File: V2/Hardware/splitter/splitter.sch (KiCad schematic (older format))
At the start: 17 parts, among them J0 Rpi_40Pin_F, J1 Control_seg:1, J2 Control_seg:2, J3 Control_seg:3, J4 Molex_PSU_F, J5 Siren, J6 USB_A_F, K0 RELRAS0515, Q1 BD139-16

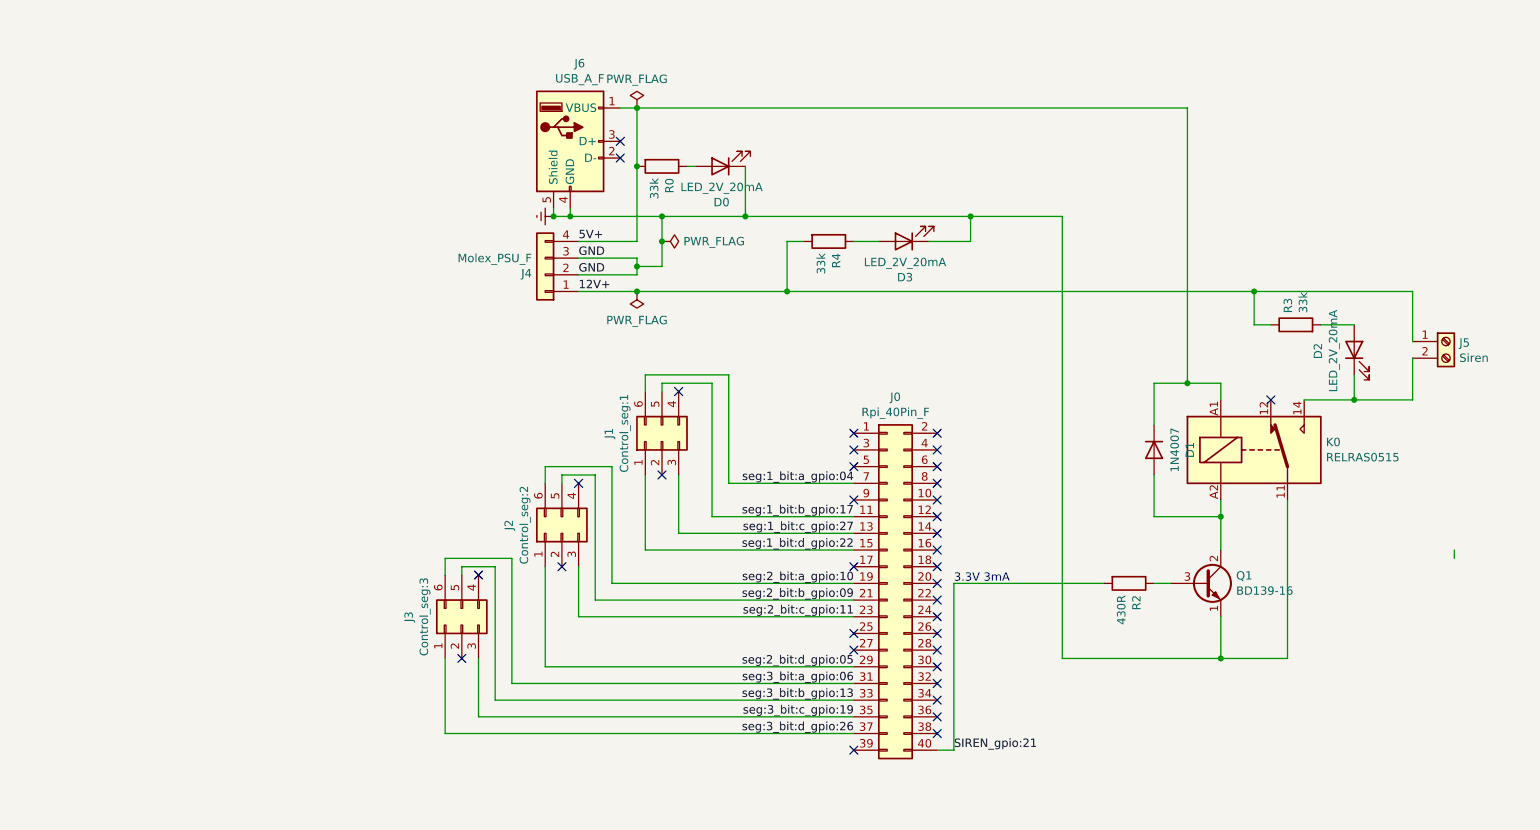
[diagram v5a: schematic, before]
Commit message: Add bypass caps and filtering
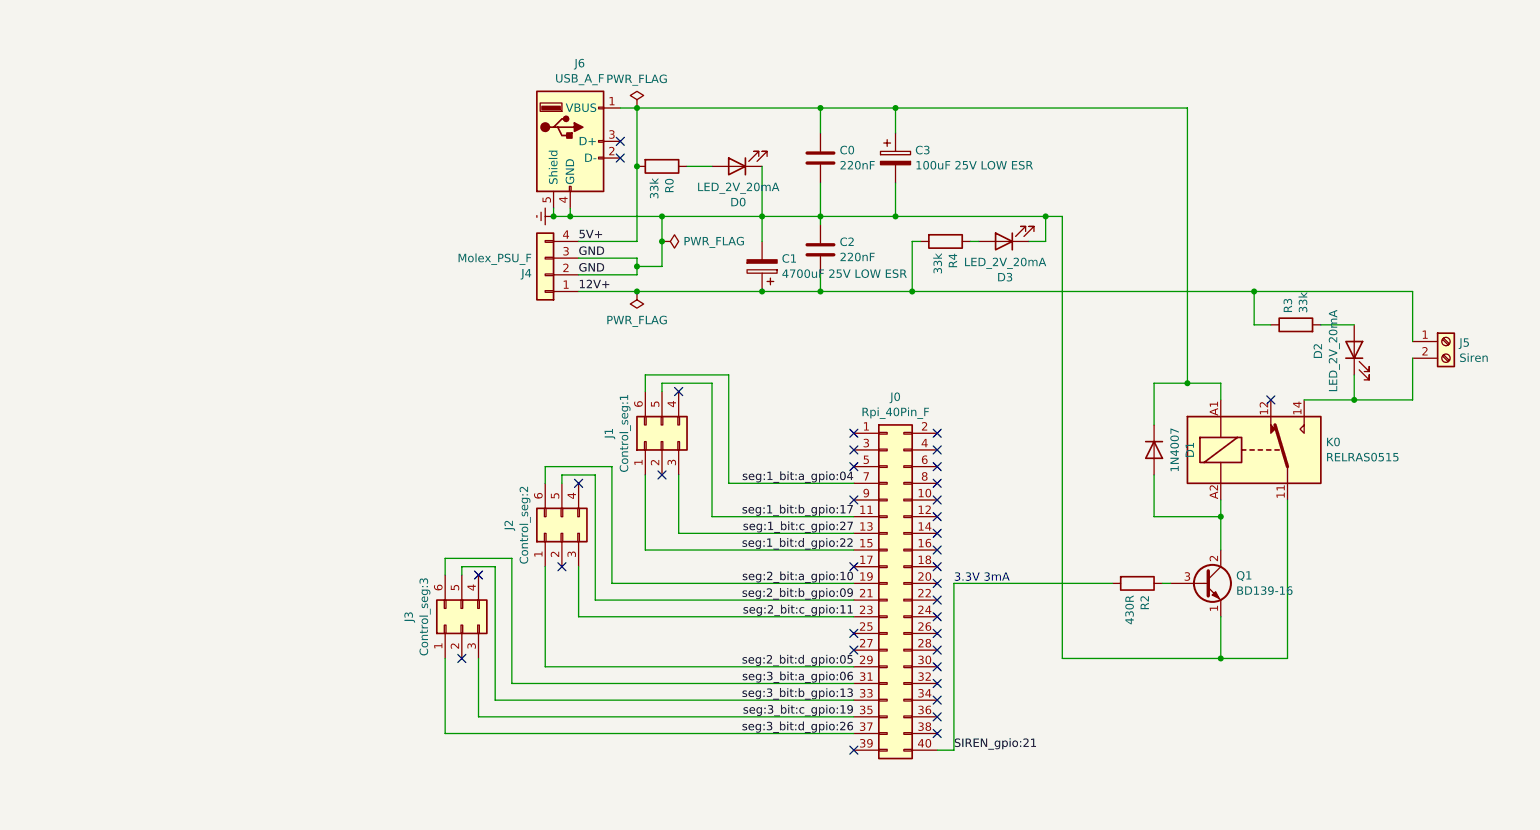
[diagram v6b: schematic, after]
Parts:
- added C0, C2: 220nF, Capacitor_THT:C_Disc_D4.3mm_W1.9mm_P5.00mm, symbol Device:C
- added C1: 4700uF 25V LOW ESR, Capacitor_THT:CP_Radial_D18.0mm_P7.50mm, symbol Device:CP
- added C3: 100uF 25V LOW ESR, Capacitor_THT:CP_Radial_D10.0mm_P5.00mm, symbol Device:CP
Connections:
- net 12V+: now also C1.1, C2.2
- net 5V+: now also C0.1, C3.1
- net Earth: now also C0.2, C1.2, C2.1, C3.2
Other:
- moved on the sheet: D0, D3, R2, R4
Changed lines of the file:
@@
 L Device:LED D0
 U 1 1 5EC196E4
-P 4800 2100
-F 0 "D0" H 4793 2316 50  0000 C CNN
-F 1 "LED_2V_20mA" H 4793 2225 50  0000 C CNN
-F 2 "LED_THT:LED_D5.0mm" H 4800 2100 50  0001 C CNN
-F 3 "~" H 4800 2100 50  0001 C CNN
-	1    4800 2100
+P 4900 2100
+F 0 "D0" H 4893 2316 50  0000 C CNN
+F 1 "LED_2V_20mA" H 4893 2225 50  0000 C CNN
+F 2 "LED_THT:LED_D5.0mm" H 4900 2100 50  0001 C CNN
+F 3 "~" H 4900 2100 50  0001 C CNN
+	1    4900 2100
 	-1   0    0    1
 $EndComp
@@
 	4450 2550 4450 2400
 Wire Wire Line
-	4450 2400 4950 2400
+	4450 2400 5050 2400
 Connection ~ 4450 2400
 Connection ~ 4300 2100
@@
 	4300 2100 4300 1750
 Wire Wire Line
-	4600 2100 4650 2100
-Wire Wire Line
-	4950 2100 4950 2400
-Connection ~ 4950 2400
+	4600 2100 4750 2100
+Wire Wire Line
+	5050 2100 5050 2400
+Connection ~ 5050 2400
 $Comp
 L power:PWR_FLAG #FLG0103
@@
 L Device:R R2
 U 1 1 5ED47928
-P 7250 4600
-F 0 "R2" H 7320 4646 50  0000 L CNN
-F 1 "430R" H 7320 4555 50  0000 L CNN
-F 2 "Resistor_THT:R_Axial_DIN0207_L6.3mm_D2.5mm_P10.16mm_Horizontal" V 7180 4600 50  0001 C CNN
-F 3 "~" H 7250 4600 50  0001 C CNN
-	1    7250 4600
+P 7300 4600
+F 0 "R2" H 7370 4646 50  0000 L CNN
+F 1 "430R" H 7370 4555 50  0000 L CNN
+F 2 "Resistor_THT:R_Axial_DIN0207_L6.3mm_D2.5mm_P10.16mm_Horizontal" V 7230 4600 50  0001 C CNN
+F 3 "~" H 7300 4600 50  0001 C CNN
+	1    7300 4600
 	0    1    1    0
 $EndComp
@@
 $EndComp
 Wire Wire Line
-	7400 4600 7500 4600
-Wire Wire Line
-	4300 2850 5200 2850
-Wire Wire Line
-	6850 2400 6850 5050
+	7450 4600 7500 4600
+Wire Wire Line
+	4300 2850 5050 2850
 Wire Wire Line
 	6850 5050 7800 5050
 Wire Wire Line
 	7800 5050 7800 4800
-Wire Wire Line
-	4950 2400 6300 2400
 Wire Wire Line
 	7800 4100 7800 4200
@@
 	0    -1   -1   0
 $EndComp
-Wire Wire Line
-	9200 4450 9200 4400
 NoConn ~ 6100 4200
 $Comp
@@
 L Device:R R4
 U 1 1 5FCA692B
-P 5450 2550
-F 0 "R4" H 5520 2596 50  0000 L CNN
-F 1 "33k" H 5520 2505 50  0000 L CNN
-F 2 "Resistor_THT:R_Axial_DIN0207_L6.3mm_D2.5mm_P10.16mm_Horizontal" V 5380 2550 50  0001 C CNN
-F 3 "~" H 5450 2550 50  0001 C CNN
-	1    5450 2550
+P 6150 2550
+F 0 "R4" H 6220 2596 50  0000 L CNN
+F 1 "33k" H 6220 2505 50  0000 L CNN
+F 2 "Resistor_THT:R_Axial_DIN0207_L6.3mm_D2.5mm_P10.16mm_Horizontal" V 6080 2550 50  0001 C CNN
+F 3 "~" H 6150 2550 50  0001 C CNN
+	1    6150 2550
 	0    1    1    0
 $EndComp
@@
 L Device:LED D3
 U 1 1 5FCABBDF
-P 5900 2550
-F 0 "D3" H 5893 2766 50  0000 C CNN
-F 1 "LED_2V_20mA" H 5893 2675 50  0000 C CNN
-F 2 "LED_THT:LED_D5.0mm" H 5900 2550 50  0001 C CNN
-F 3 "~" H 5900 2550 50  0001 C CNN
-	1    5900 2550
+P 6500 2550
+F 0 "D3" H 6493 2766 50  0000 C CNN
+F 1 "LED_2V_20mA" H 6493 2675 50  0000 C CNN
+F 2 "LED_THT:LED_D5.0mm" H 6500 2550 50  0001 C CNN
+F 3 "~" H 6500 2550 50  0001 C CNN
+	1    6500 2550
 	-1   0    0    1
 $EndComp
 Wire Wire Line
-	5200 2850 5200 2550
-Wire Wire Line
-	5200 2550 5300 2550
-Connection ~ 5200 2850
-Wire Wire Line
-	5600 2550 5750 2550
-Wire Wire Line
-	6050 2550 6300 2550
-Wire Wire Line
-	6300 2550 6300 2400
-Connection ~ 6300 2400
-Wire Wire Line
-	6300 2400 6850 2400
+	5950 2850 5950 2550
+Wire Wire Line
+	5950 2550 6000 2550
+Connection ~ 5950 2850
+Wire Wire Line
+	6300 2550 6350 2550
+Wire Wire Line
+	6650 2550 6750 2550
+Wire Wire Line
+	6750 2550 6750 2400
+Connection ~ 6750 2400
+Wire Wire Line
+	6750 2400 6850 2400
 Wire Wire Line
 	4850 4000 5600 4000
@@
 NoConn ~ 3250 5050
 Wire Wire Line
-	6200 4600 7100 4600
+	6200 4600 7150 4600
 Wire Wire Line
 	7600 3400 7600 1750
 Wire Wire Line
-	4300 1750 7600 1750
+	4300 1750 5400 1750
 Connection ~ 7600 3400
 Wire Wire Line
@@
 Wire Wire Line
 	8950 2850 8950 3150
-Wire Wire Line
-	5200 2850 8000 2850
 Wire Wire Line
 	8300 3500 8600 3500
@@
 Text Notes 6200 4600 0    50   ~ 0
 3.3V 3mA
+$Comp
+L Device:CP C1
+U 1 1 5FDD03EF
+P 5050 2700
+F 0 "C1" H 4932 2654 50  0000 R CNN
+F 1 "4700uF 25V LOW ESR" H 4932 2745 50  0000 R CNN
+F 2 "Capacitor_THT:CP_Radial_D18.0mm_P7.50mm" H 5088 2550 50  0001 C CNN
+F 3 "~" H 5050 2700 50  0001 C CNN
+	1    5050 2700
+	-1   0    0    1
+$EndComp
+Wire Wire Line
+	5050 2550 5050 2400
+Wire Wire Line
+	5050 2400 5400 2400
+Connection ~ 5050 2850
+Wire Wire Line
+	5050 2850 5400 2850
+$Comp
+L Device:C C2
+U 1 1 5FE2424F
+P 5400 2600
+F 0 "C2" H 5515 2646 50  0000 L CNN
+F 1 "220nF" H 5515 2555 50  0000 L CNN
+F 2 "Capacitor_THT:C_Disc_D4.3mm_W1.9mm_P5.00mm" H 5438 2450 50  0001 C CNN
+F 3 "~" H 5400 2600 50  0001 C CNN
+	1    5400 2600
+	1    0    0    -1
+$EndComp
+Wire Wire Line
+	5400 2450 5400 2400
+Connection ~ 5400 2400
+Wire Wire Line
+	5400 2400 5850 2400
+Wire Wire Line
+	5400 2750 5400 2850
+Connection ~ 5400 2850
+Wire Wire Line
+	5400 2850 5950 2850
+$Comp
+L Device:C C0
+U 1 1 5FE2BD03
+P 5400 2050
+F 0 "C0" H 5515 2096 50  0000 L CNN
+F 1 "220nF" H 5515 2005 50  0000 L CNN
+F 2 "Capacitor_THT:C_Disc_D4.3mm_W1.9mm_P5.00mm" H 5438 1900 50  0001 C CNN
+F 3 "~" H 5400 2050 50  0001 C CNN
+	1    5400 2050
+	1    0    0    -1
+$EndComp
+Connection ~ 5400 1750
+Wire Wire Line
+	5400 1750 5850 1750
+Wire Wire Line
+	5400 1750 5400 1900
+Wire Wire Line
+	5400 2200 5400 2400
+$Comp
+L Device:CP C3
+U 1 1 5FE36909
+P 5850 2050
+F 0 "C3" H 5968 2096 50  0000 L CNN
+F 1 "100uF 25V LOW ESR" H 5968 2005 50  0000 L CNN
+F 2 "Capacitor_THT:CP_Radial_D10.0mm_P5.00mm" H 5888 1900 50  0001 C CNN
+F 3 "~" H 5850 2050 50  0001 C CNN
+	1    5850 2050
+	1    0    0    -1
+$EndComp
+Wire Wire Line
+	5850 1900 5850 1750
+Connection ~ 5850 1750
+Wire Wire Line
+	5850 1750 7600 1750
+Wire Wire Line
+	5850 2200 5850 2400
+Connection ~ 5850 2400
+Wire Wire Line
+	5850 2400 6750 2400
+Wire Wire Line
+	5950 2850 8000 2850
+Wire Wire Line
+	6850 2400 6850 5050
 $EndSCHEMATC

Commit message: Update splitter
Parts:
- removed C1: 4700uF 25V LOW ESR, Capacitor_THT:CP_Radial_D18.0mm_P7.50mm, symbol Device:CP
- removed C2: 220nF, Capacitor_THT:C_Disc_D4.3mm_W1.9mm_P5.00mm, symbol Device:C
- removed D3: LED_2V_20mA, LED_THT:LED_D5.0mm, symbol Device:LED
- removed R3, R4: 33k, Resistor_THT:R_Axial_DIN0207_L6.3mm_D2.5mm_P10.16mm_Horizontal, symbol Device:R
- added J7: Siren, TerminalBlock_RND:TerminalBlock_RND_205-00067_1x02_P7.50mm_Horizontal, symbol Connector:Screw_Terminal_01x02
- added R1: 33k, Resistor_THT:R_Axial_DIN0207_L6.3mm_D2.5mm_P10.16mm_Horizontal, symbol Device:R
- J6: renamed from J5; footprint TerminalBlock:TerminalBlock_bornier-2_P5.08mm -> TerminalBlock_RND:TerminalBlock_RND_205-00067_1x02_P7.50mm_Horizontal
- renumbered J6 to J5
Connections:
- net 12V+: no longer J6.1 (Pin_1)
- net 5V+: now also R1.2
- net Earth: no longer K0.11
- net at D1.2 (A), K0.A2, Q1.2 (C): now also D2.1 (K)
- net at D2.2 (A): now also R1.1
- new net: J7.1 (Pin_1), K0.11
- new net 230V-L: J6.1 (Pin_1), K0.14
- new net 230V-N: J6.2 (Pin_2), J7.2 (Pin_2)
- no-connect marks 36 -> 37
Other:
- moved on the sheet: D0, J6, R0
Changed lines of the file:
@@
 $EndComp
 $Comp
-L splitter-rescue:USB_A-Connector J6
+L splitter-rescue:USB_A-Connector J5
 U 1 1 5EBB092E
 P 3900 1950
-F 0 "J6" H 3957 2417 50  0000 C CNN
+F 0 "J5" H 3957 2417 50  0000 C CNN
 F 1 "USB_A_F" H 3957 2326 50  0000 C CNN
 F 2 "Connector_USB:USB_A_Stewart_SS-52100-001_Horizontal" H 4050 1900 50  0001 C CNN
@@
 $EndComp
 $Comp
-L Connector:Screw_Terminal_01x02 J5
+L Connector:Screw_Terminal_01x02 J6
 U 1 1 5EBB14C8
-P 9150 3150
-F 0 "J5" H 9230 3142 50  0000 L CNN
-F 1 "Siren" H 9230 3051 50  0000 L CNN
-F 2 "TerminalBlock:TerminalBlock_bornier-2_P5.08mm" H 9150 3150 50  0001 C CNN
-F 3 "~" H 9150 3150 50  0001 C CNN
-	1    9150 3150
+P 9300 3150
+F 0 "J6" H 9380 3142 50  0000 L CNN
+F 1 "Siren" H 9380 3051 50  0000 L CNN
+F 2 "TerminalBlock_RND:TerminalBlock_RND_205-00067_1x02_P7.50mm_Horizontal" H 9300 3150 50  0001 C CNN
+F 3 "~" H 9300 3150 50  0001 C CNN
+	1    9300 3150
 	1    0    0    -1
 $EndComp
@@
 L Device:R R0
 U 1 1 5EC190C2
-P 4450 2100
-F 0 "R0" H 4520 2146 50  0000 L CNN
-F 1 "33k" H 4520 2055 50  0000 L CNN
-F 2 "Resistor_THT:R_Axial_DIN0207_L6.3mm_D2.5mm_P10.16mm_Horizontal" V 4380 2100 50  0001 C CNN
-F 3 "~" H 4450 2100 50  0001 C CNN
-	1    4450 2100
+P 4550 2100
+F 0 "R0" H 4620 2146 50  0000 L CNN
+F 1 "33k" H 4620 2055 50  0000 L CNN
+F 2 "Resistor_THT:R_Axial_DIN0207_L6.3mm_D2.5mm_P10.16mm_Horizontal" V 4480 2100 50  0001 C CNN
+F 3 "~" H 4550 2100 50  0001 C CNN
+	1    4550 2100
 	0    1    1    0
 $EndComp
@@
 L Device:LED D0
 U 1 1 5EC196E4
-P 4900 2100
-F 0 "D0" H 4893 2316 50  0000 C CNN
-F 1 "LED_2V_20mA" H 4893 2225 50  0000 C CNN
-F 2 "LED_THT:LED_D5.0mm" H 4900 2100 50  0001 C CNN
-F 3 "~" H 4900 2100 50  0001 C CNN
-	1    4900 2100
+P 5000 2100
+F 0 "D0" H 4993 2316 50  0000 C CNN
+F 1 "LED_2V_20mA" H 4993 2225 50  0000 C CNN
+F 2 "LED_THT:LED_D5.0mm" H 5000 2100 50  0001 C CNN
+F 3 "~" H 5000 2100 50  0001 C CNN
+	1    5000 2100
 	-1   0    0    1
 $EndComp
@@
 	4300 2750 3950 2750
 Wire Wire Line
-	3950 2850 4300 2850
-Wire Wire Line
 	3950 2550 4300 2550
-Wire Wire Line
-	4300 2550 4300 2100
 Wire Wire Line
 	4300 1750 4200 1750
@@
 $EndComp
 Connection ~ 3800 2400
-$Comp
-L power:PWR_FLAG #FLG0102
-U 1 1 5EC7A631
-P 4300 2850
-F 0 "#FLG0102" H 4300 2925 50  0001 C CNN
-F 1 "PWR_FLAG" H 4300 3023 50  0000 C CNN
-F 2 "" H 4300 2850 50  0001 C CNN
-F 3 "~" H 4300 2850 50  0001 C CNN
-	1    4300 2850
-	-1   0    0    1
-$EndComp
-Connection ~ 4300 2850
 NoConn ~ 4200 1950
 NoConn ~ 4200 2050
@@
 	4450 2550 4450 2400
 Wire Wire Line
-	4450 2400 5050 2400
+	4450 2400 5150 2400
 Connection ~ 4450 2400
-Connection ~ 4300 2100
-Wire Wire Line
-	4300 2100 4300 1750
-Wire Wire Line
-	4600 2100 4750 2100
-Wire Wire Line
-	5050 2100 5050 2400
-Connection ~ 5050 2400
+Wire Wire Line
+	5150 2100 5150 2400
+Connection ~ 5150 2400
 $Comp
 L power:PWR_FLAG #FLG0103
@@
 	7450 4600 7500 4600
 Wire Wire Line
-	4300 2850 5050 2850
-Wire Wire Line
 	6850 5050 7800 5050
 Wire Wire Line
@@
 Wire Wire Line
 	7800 3400 7800 3500
-Wire Wire Line
-	8200 4100 8200 5050
-Wire Wire Line
-	8200 5050 7800 5050
-Connection ~ 7800 5050
 NoConn ~ 8100 3500
 NoConn ~ 6100 4100
-$Comp
-L Device:LED D2
-U 1 1 5EDC36BC
-P 8600 3200
-F 0 "D2" H 8593 3416 50  0000 C CNN
-F 1 "LED_2V_20mA" H 8593 3325 50  0000 C CNN
-F 2 "LED_THT:LED_D5.0mm" H 8600 3200 50  0001 C CNN
-F 3 "~" H 8600 3200 50  0001 C CNN
-	1    8600 3200
-	0    -1   -1   0
-$EndComp
-$Comp
-L Device:R R3
-U 1 1 5EDC8D2F
-P 8250 3050
-F 0 "R3" H 8320 3096 50  0000 L CNN
-F 1 "33k" H 8320 3005 50  0000 L CNN
-F 2 "Resistor_THT:R_Axial_DIN0207_L6.3mm_D2.5mm_P10.16mm_Horizontal" V 8180 3050 50  0001 C CNN
-F 3 "~" H 8250 3050 50  0001 C CNN
-	1    8250 3050
-	0    -1   -1   0
-$EndComp
 NoConn ~ 6100 4200
 $Comp
@@
 Wire Wire Line
 	3450 5300 5600 5300
-$Comp
-L Device:R R4
-U 1 1 5FCA692B
-P 6150 2550
-F 0 "R4" H 6220 2596 50  0000 L CNN
-F 1 "33k" H 6220 2505 50  0000 L CNN
-F 2 "Resistor_THT:R_Axial_DIN0207_L6.3mm_D2.5mm_P10.16mm_Horizontal" V 6080 2550 50  0001 C CNN
-F 3 "~" H 6150 2550 50  0001 C CNN
-	1    6150 2550
-	0    1    1    0
-$EndComp
-$Comp
-L Device:LED D3
-U 1 1 5FCABBDF
-P 6500 2550
-F 0 "D3" H 6493 2766 50  0000 C CNN
-F 1 "LED_2V_20mA" H 6493 2675 50  0000 C CNN
-F 2 "LED_THT:LED_D5.0mm" H 6500 2550 50  0001 C CNN
-F 3 "~" H 6500 2550 50  0001 C CNN
-	1    6500 2550
-	-1   0    0    1
-$EndComp
-Wire Wire Line
-	5950 2850 5950 2550
-Wire Wire Line
-	5950 2550 6000 2550
-Connection ~ 5950 2850
-Wire Wire Line
-	6300 2550 6350 2550
-Wire Wire Line
-	6650 2550 6750 2550
-Wire Wire Line
-	6750 2550 6750 2400
-Connection ~ 6750 2400
-Wire Wire Line
-	6750 2400 6850 2400
 Wire Wire Line
 	4850 4000 5600 4000
@@
 	6200 4600 7150 4600
 Wire Wire Line
-	7600 3400 7600 1750
+	7600 3400 7600 3100
 Wire Wire Line
 	4300 1750 5400 1750
@@
 Wire Wire Line
 	7600 3400 7400 3400
-Wire Wire Line
-	8950 2850 8950 3150
-Wire Wire Line
-	8300 3500 8600 3500
-Wire Wire Line
-	8950 3500 8950 3250
-Wire Wire Line
-	8600 3050 8400 3050
-Wire Wire Line
-	8100 3050 8000 3050
-Wire Wire Line
-	8000 3050 8000 2850
-Connection ~ 8000 2850
-Wire Wire Line
-	8000 2850 8950 2850
-Wire Wire Line
-	8600 3350 8600 3500
-Connection ~ 8600 3500
-Wire Wire Line
-	8600 3500 8950 3500
 Text Notes 6200 4600 0    50   ~ 0
 3.3V 3mA
-$Comp
-L Device:CP C1
-U 1 1 5FDD03EF
-P 5050 2700
-F 0 "C1" H 4932 2654 50  0000 R CNN
-F 1 "4700uF 25V LOW ESR" H 4932 2745 50  0000 R CNN
-F 2 "Capacitor_THT:CP_Radial_D18.0mm_P7.50mm" H 5088 2550 50  0001 C CNN
-F 3 "~" H 5050 2700 50  0001 C CNN
-	1    5050 2700
-	-1   0    0    1
-$EndComp
-Wire Wire Line
-	5050 2550 5050 2400
-Wire Wire Line
-	5050 2400 5400 2400
-Connection ~ 5050 2850
-Wire Wire Line
-	5050 2850 5400 2850
-$Comp
-L Device:C C2
-U 1 1 5FE2424F
-P 5400 2600
-F 0 "C2" H 5515 2646 50  0000 L CNN
-F 1 "220nF" H 5515 2555 50  0000 L CNN
-F 2 "Capacitor_THT:C_Disc_D4.3mm_W1.9mm_P5.00mm" H 5438 2450 50  0001 C CNN
-F 3 "~" H 5400 2600 50  0001 C CNN
-	1    5400 2600
-	1    0    0    -1
-$EndComp
-Wire Wire Line
-	5400 2450 5400 2400
+Wire Wire Line
+	5150 2400 5400 2400
 Connection ~ 5400 2400
 Wire Wire Line
 	5400 2400 5850 2400
-Wire Wire Line
-	5400 2750 5400 2850
-Connection ~ 5400 2850
-Wire Wire Line
-	5400 2850 5950 2850
 $Comp
 L Device:C C0
@@
 Connection ~ 5850 2400
 Wire Wire Line
-	5850 2400 6750 2400
-Wire Wire Line
-	5950 2850 8000 2850
-Wire Wire Line
 	6850 2400 6850 5050
+Wire Wire Line
+	5850 2400 6850 2400
+NoConn ~ 3950 2850
+Wire Wire Line
+	4300 1750 4300 2100
+Wire Wire Line
+	4700 2100 4850 2100
+Wire Wire Line
+	4400 2100 4300 2100
+Connection ~ 4300 2100
+Wire Wire Line
+	4300 2100 4300 2550
+$Comp
+L Connector:Screw_Terminal_01x02 J7
+U 1 1 60876BBF
+P 9300 4200
+F 0 "J7" H 9380 4192 50  0000 L CNN
+F 1 "Siren" H 9380 4101 50  0000 L CNN
+F 2 "TerminalBlock_RND:TerminalBlock_RND_205-00067_1x02_P7.50mm_Horizontal" H 9300 4200 50  0001 C CNN
+F 3 "~" H 9300 4200 50  0001 C CNN
+	1    9300 4200
+	1    0    0    -1
+$EndComp
+Text Label 9000 3650 0    50   ~ 0
+230V-N
+Text Label 8300 3150 0    50   ~ 0
+230V-L
+$Comp
+L Device:LED D2
+U 1 1 60899463
+P 7150 3800
+F 0 "D2" H 7143 4016 50  0000 C CNN
+F 1 "LED_2V_20mA" H 7143 3925 50  0000 C CNN
+F 2 "LED_THT:LED_D5.0mm" H 7150 3800 50  0001 C CNN
+F 3 "~" H 7150 3800 50  0001 C CNN
+	1    7150 3800
+	0    -1   -1   0
+$EndComp
+$Comp
+L Device:R R1
+U 1 1 6089AC25
+P 7150 3350
+F 0 "R1" H 7220 3396 50  0000 L CNN
+F 1 "33k" H 7220 3305 50  0000 L CNN
+F 2 "Resistor_THT:R_Axial_DIN0207_L6.3mm_D2.5mm_P10.16mm_Horizontal" V 7080 3350 50  0001 C CNN
+F 3 "~" H 7150 3350 50  0001 C CNN
+	1    7150 3350
+	-1   0    0    1
+$EndComp
+Wire Wire Line
+	7150 3650 7150 3500
+Wire Wire Line
+	7150 3200 7150 3100
+Wire Wire Line
+	7150 3100 7600 3100
+Connection ~ 7600 3100
+Wire Wire Line
+	7600 3100 7600 1750
+Wire Wire Line
+	7150 3950 7150 4200
+Wire Wire Line
+	7150 4200 7400 4200
+Connection ~ 7400 4200
+Wire Wire Line
+	8200 4100 8200 4200
+Wire Wire Line
+	8200 4200 9100 4200
+Wire Wire Line
+	8300 3500 8300 3150
+Wire Wire Line
+	8300 3150 9100 3150
+Wire Wire Line
+	9100 3250 9000 3250
+Wire Wire Line
+	9000 3250 9000 4300
+Wire Wire Line
+	9000 4300 9100 4300
 $EndSCHEMATC
